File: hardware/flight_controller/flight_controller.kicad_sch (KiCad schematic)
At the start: 13 parts, among them J1 Conn_02x04_Odd_Even, J2 Conn_01x03, J3 Conn_01x03, J4 Conn_01x03, J5 Conn_01x03, J6 Conn_01x05, J7 Conn_01x03, U1 Teensy3.6, U2 Logic_Level_Converter, U3 Logic_Level_Converter

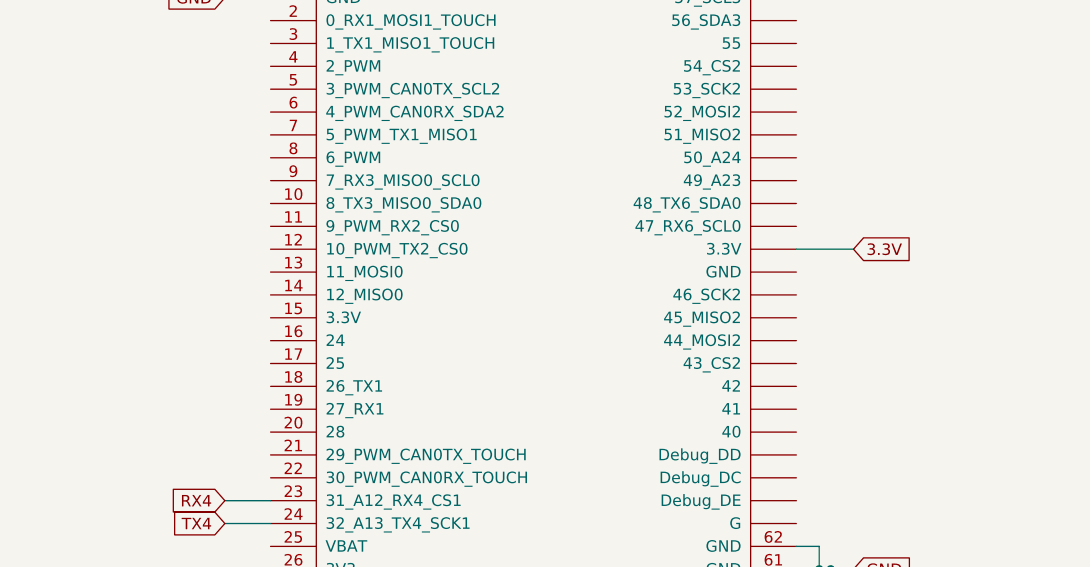
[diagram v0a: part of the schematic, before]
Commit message: Fixes PCB for v1.1, gets logging working in firmawre, adds data viewing in jupyter notebooks
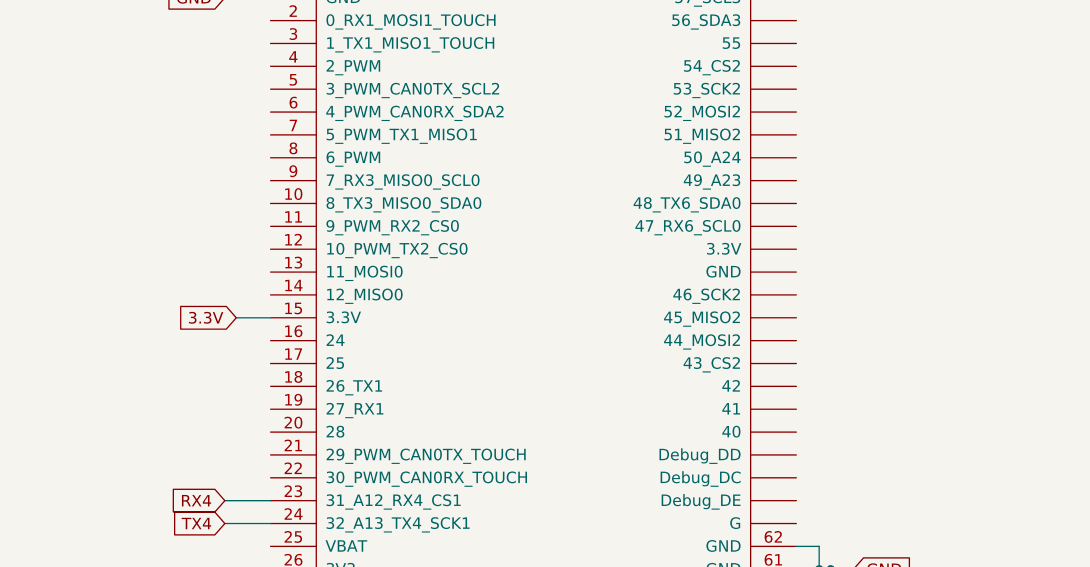
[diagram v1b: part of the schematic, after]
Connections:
- net 3.3V: now also U1.15 (3.3V); no longer U1.~ (GND)
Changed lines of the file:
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@@
+    (stroke (width 0) (type default) (color 0 0 0 0))
+  )
+  (wire (pts (xy 111.76 63.5) (xy 115.57 63.5))
     (stroke (width 0) (type default) (color 0 0 0 0))
   )
@@
   )
   (wire (pts (xy 257.81 107.95) (xy 257.81 110.49))
-    (stroke (width 0) (type default) (color 0 0 0 0))
-  )
-  (wire (pts (xy 173.99 55.88) (xy 180.34 55.88))
     (stroke (width 0) (type default) (color 0 0 0 0))
   )
@@
     )
   )
-  (global_label "3.3V" (shape input) (at 180.34 55.88 0) (fields_autoplaced)
-    (effects (font (size 1.27 1.27)) (justify left))
-    (property "Intersheet References" "${INTERSHEET_REFS}" (id 0) (at 186.8655 55.8006 0)
-      (effects (font (size 1.27 1.27)) (justify left) hide)
-    )
-  )
+  (global_label "3.3V" (shape input) (at 111.76 63.5 180) (fields_autoplaced)
+    (effects (font (size 1.27 1.27)) (justify right))
+    (property "Intersheet References" "${INTERSHEET_REFS}" (id 0) (at 105.2345 63.5794 0)
+      (effects (font (size 1.27 1.27)) (justify right) hide)
+    )
+  )

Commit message: PID gain tuning, but the front right motor is getting hot and might be a problem
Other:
- title: (none) -> Flight Controller
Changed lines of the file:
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@@
 (kicad_sch (version 20211123) (generator eeschema)
   (paper "A4")
+  (title_block
+    (title "Flight Controller")
+    (rev "1.1")
+  )
   (junction (at 257.81 107.95) (diameter 0) (color 0 0 0 0)
   )
